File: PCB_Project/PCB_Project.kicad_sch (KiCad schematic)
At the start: 7 parts

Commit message: working on final board
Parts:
- renumbered R4 to R1, R5 to R2, R2 to R3, R1 to R4, R9 to R5, R8 to R6, U4 to U1
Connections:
- net GND: no longer U1.9 (GND)
- net I2C_SCL_M: no longer U1.28 (GPIO_1)
- net I2C_SDA_M: no longer U1.27 (GPIO_0)
- net Pi_TX: now also U1.36 (GPIO_16); no longer U1.8 (GPIO_14)
- net CSB_Accel_BMI088_1: now reaches U1.24 (GPIO_8)
- net CSB_Accel_BMI088 renamed CSB_Gryo_BMI088_1
- net CSB_Gryo_BMI088 renamed CSB_Gryo_BMI088_2
- net SCLK_2 renamed SCK_2
- net SDI_1 renamed MOSI_1
- net SDI_2 renamed MOSI_2
- net SDO_1 renamed MISO_1
- net SDO_2 renamed MISO_2
- net nCS_2 renamed CSB_Accel_BMI088_2
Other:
- added sheet Level Shifters (Level_Shifters.kicad_sch)
- added sheet Power Management (Power_Management.kicad_sch)
- moved on the sheet: R1, R2, R3, R4, R5, R6, U1

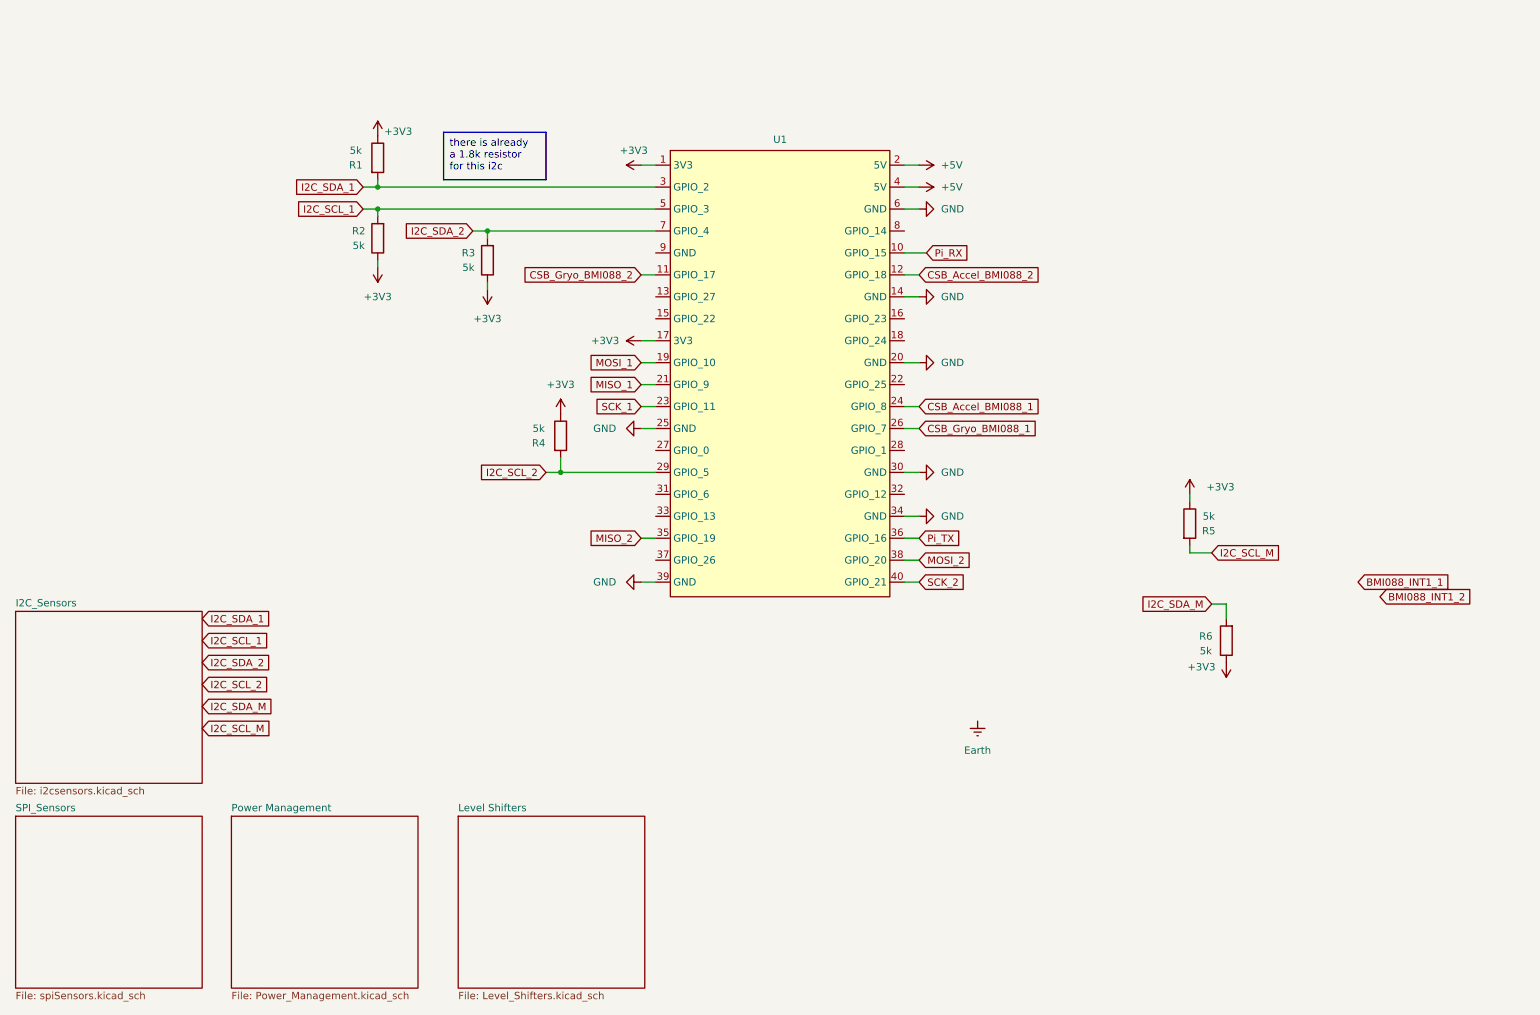
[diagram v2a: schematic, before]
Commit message: power distribution done
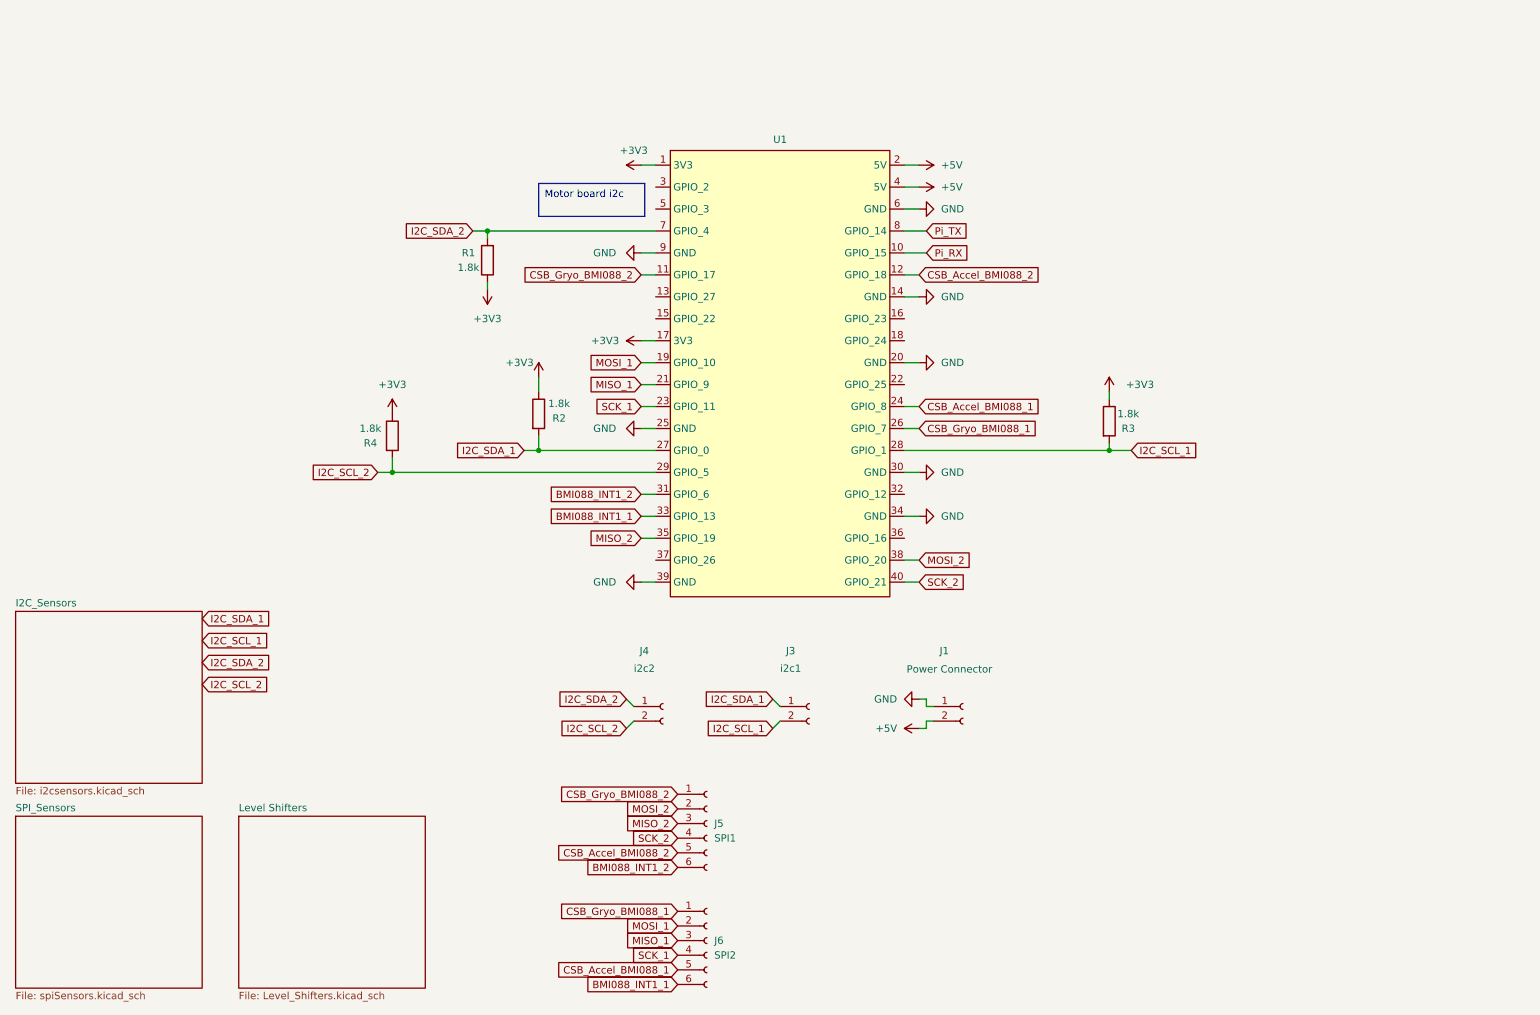
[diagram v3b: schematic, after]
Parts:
- removed R1, R2: 5k, Resistor_SMD:R_0402_1005Metric, symbol Device:R
- added J1: Power Connector, Connector_JST:JST_PH_B2B-PH-K_1x02_P2.00mm_Vertical, symbol Connector:Conn_01x02_Socket
- added J3: i2c1, Connector_JST:JST_PH_B2B-PH-K_1x02_P2.00mm_Vertical, symbol Connector:Conn_01x02_Socket
- added J4: i2c2, Connector_JST:JST_PH_B2B-PH-K_1x02_P2.00mm_Vertical, symbol Connector:Conn_01x02_Socket
- added J5: SPI1, Connector_PinHeader_2.54mm:PinHeader_1x06_P2.54mm_Vertical, symbol Connector:Conn_01x06_Socket
- added J6: SPI2, Connector_PinHeader_2.54mm:PinHeader_1x06_P2.54mm_Vertical, symbol Connector:Conn_01x06_Socket
- R1: renamed from R3; value 5k -> 1.8k; footprint Resistor_SMD:R_0402_1005Metric -> Resistor_SMD:R_0805_2012Metric
- R2: renamed from R6; value 5k -> 1.8k; footprint Resistor_SMD:R_0402_1005Metric -> Resistor_SMD:R_0805_2012Metric
- R3: renamed from R5; value 5k -> 1.8k; footprint Resistor_SMD:R_0402_1005Metric -> Resistor_SMD:R_0805_2012Metric
- R4: value 5k -> 1.8k; footprint Resistor_SMD:R_0402_1005Metric -> Resistor_SMD:R_0805_2012Metric
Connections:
- net I2C_SCL_M is gone; now on net I2C_SCL_1: R3.2
- net I2C_SDA_M is gone; now on net I2C_SDA_1: R2.2
- net +5V: now also J1.2 (Pin_2)
- net BMI088_INT1_1: now also U1.33 (GPIO_13), J6.6 (Pin_6)
- net BMI088_INT1_2: now also U1.31 (GPIO_6), J5.6 (Pin_6)
- net CSB_Accel_BMI088_1: now also J6.5 (Pin_5)
- net CSB_Accel_BMI088_2: now also J5.5 (Pin_5)
- net CSB_Gryo_BMI088_1: now also J6.1 (Pin_1)
- net CSB_Gryo_BMI088_2: now also J5.1 (Pin_1)
- net GND: now also U1.9 (GND), J1.1 (Pin_1)
- net I2C_SCL_1: now also U1.28 (GPIO_1), J3.2 (Pin_2); no longer U1.5 (GPIO_3)
- net I2C_SCL_2: now also J4.2 (Pin_2)
- net I2C_SDA_1: now also U1.27 (GPIO_0), J3.1 (Pin_1); no longer U1.3 (GPIO_2)
- net I2C_SDA_2: now also J4.1 (Pin_1)
- net MISO_1: now also J6.3 (Pin_3)
- net MISO_2: now also J5.3 (Pin_3)
- net MOSI_1: now also J6.2 (Pin_2)
- net MOSI_2: now also J5.2 (Pin_2)
- net Pi_TX: now also U1.8 (GPIO_14); no longer U1.36 (GPIO_16)
- net SCK_1: now also J6.4 (Pin_4)
- net SCK_2: now also J5.4 (Pin_4)
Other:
- removed sheet Power Management
- moved on the sheet: R2, R3, R4

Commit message: power baby
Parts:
- removed J1: Power Connector, Connector_JST:JST_PH_B2B-PH-K_1x02_P2.00mm_Vertical, symbol Connector:Conn_01x02_Socket
- renumbered J4 to J1, J3 to J2, J5 to J3, J6 to J4
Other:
- added sheet Power Distribution (Power_Distribution.kicad_sch)
- moved on the sheet: J1, J2, J3, J4, R1, R2, R3, R4, U1

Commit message: working on pcb
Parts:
- renumbered J3 to J1, J1 to J2, J2 to J3
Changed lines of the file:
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@@
 		(on_board yes)
 		(dnp no)
-		(property "Reference" "J2"
+		(property "Reference" "J3"
 			(at 230.886 133.858 0)
 			(effects
@@
 			(project "PCB_Project"
 				(path "/3dbd20c6-0b48-4a74-89bd-dd4c54711bfb"
-					(reference "J2")
+					(reference "J3")
 					(unit 1)
 				)
@@
 		(dnp no)
 		(fields_autoplaced yes)
-		(property "Reference" "J3"
+		(property "Reference" "J1"
 			(at 275.59 130.8099 0)
 			(effects
@@
 			(project "PCB_Project"
 				(path "/3dbd20c6-0b48-4a74-89bd-dd4c54711bfb"
-					(reference "J3")
+					(reference "J1")
 					(unit 1)
 				)
@@
 		(on_board yes)
 		(dnp no)
-		(property "Reference" "J1"
+		(property "Reference" "J2"
 			(at 205.486 133.858 0)
 			(effects
@@
 			(project "PCB_Project"
 				(path "/3dbd20c6-0b48-4a74-89bd-dd4c54711bfb"
-					(reference "J1")
-					(unit 1)
-				)
+					(reference "J2")
+					(unit 1)
+				)

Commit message: finally
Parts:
- added H1, H2, H3, H4: MountingHole_Pad, MountingHole:MountingHole_2.5mm_Pad, symbol Mechanical:MountingHole_Pad
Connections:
- net GND: now also H1.1, H2.1, H3.1, H4.1
- net S3_PWM: now reaches U1.13 (GPIO_27)
- net S4_PWM: now reaches U1.15 (GPIO_22)
- net S1_PWM: now reaches U1.16 (GPIO_23)
- net S2_PWM: now reaches U1.18 (GPIO_24)
- net ADT_INT: now reaches U1.32 (GPIO_12)
- net +5V renamed +5.25V
